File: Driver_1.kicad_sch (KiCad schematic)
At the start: 34 parts

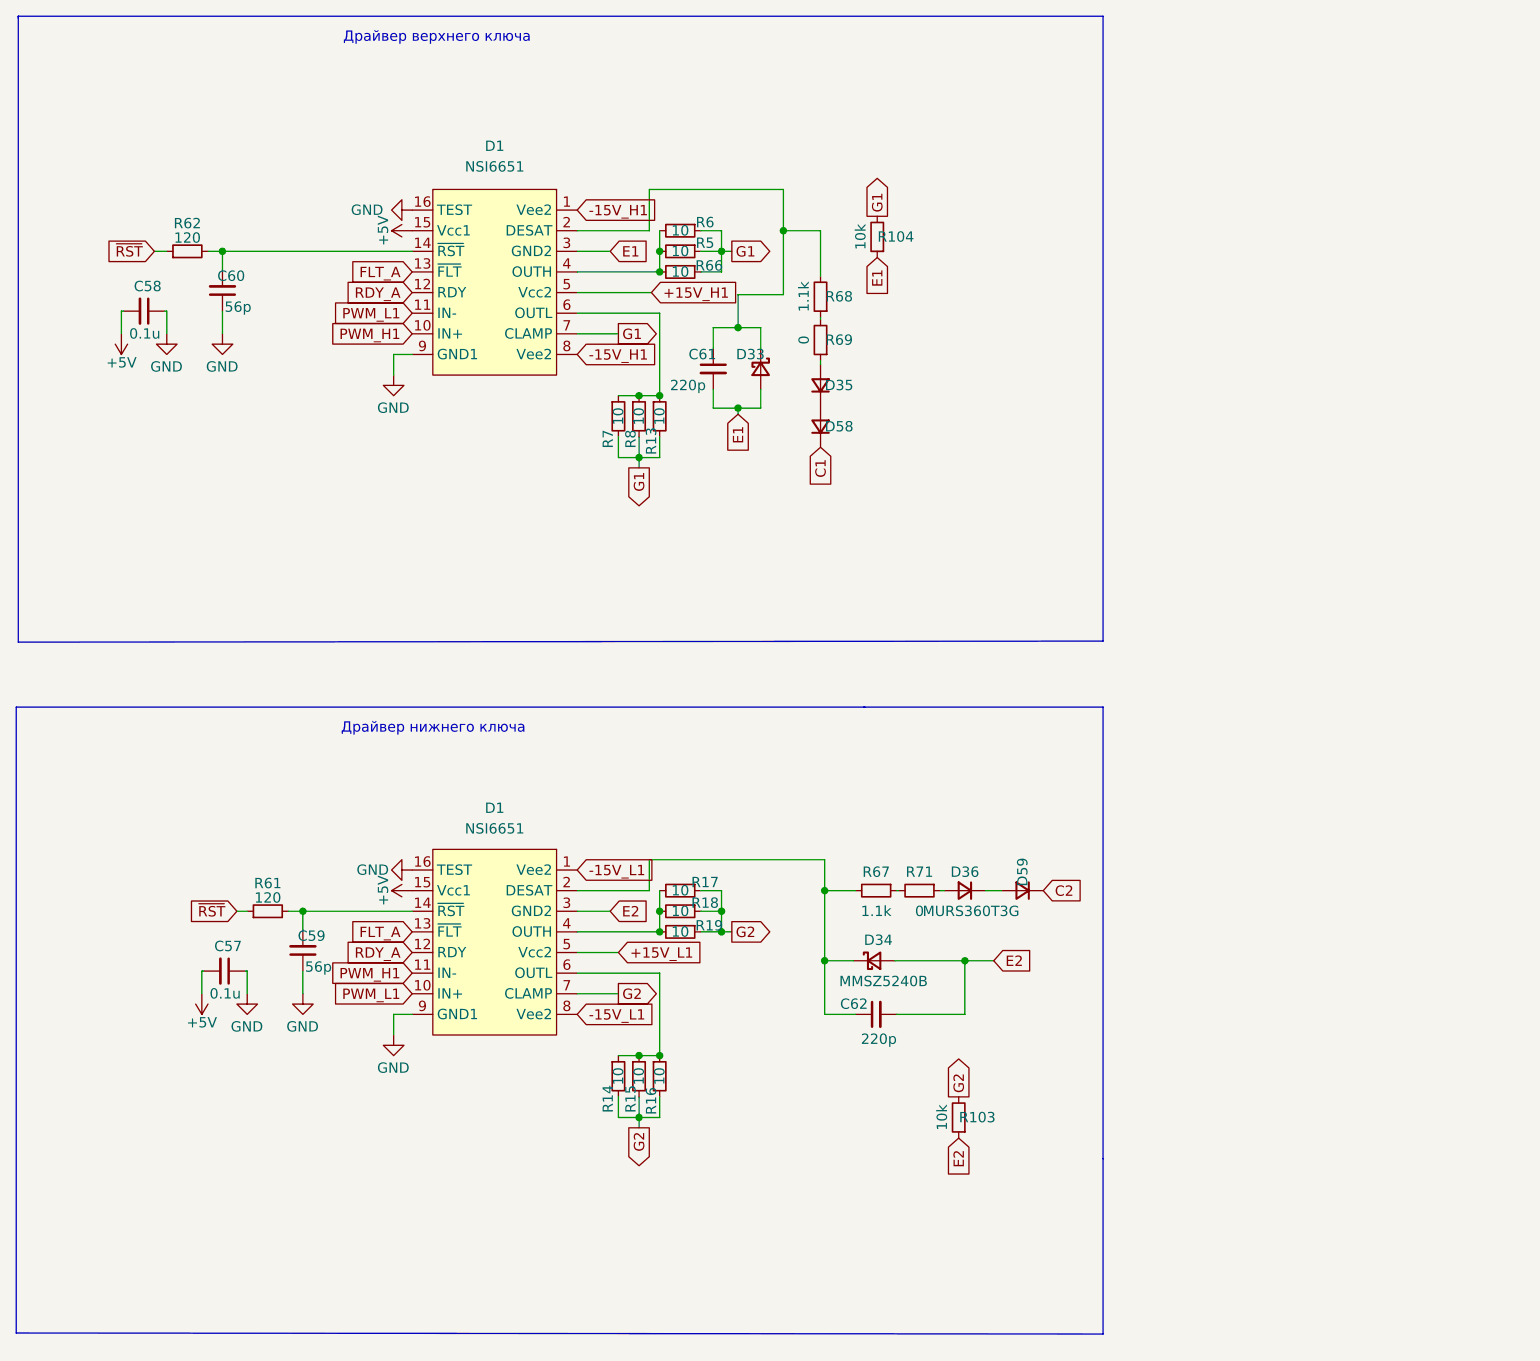
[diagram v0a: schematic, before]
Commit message: Отправил на проверку в резонит: изменил BOM
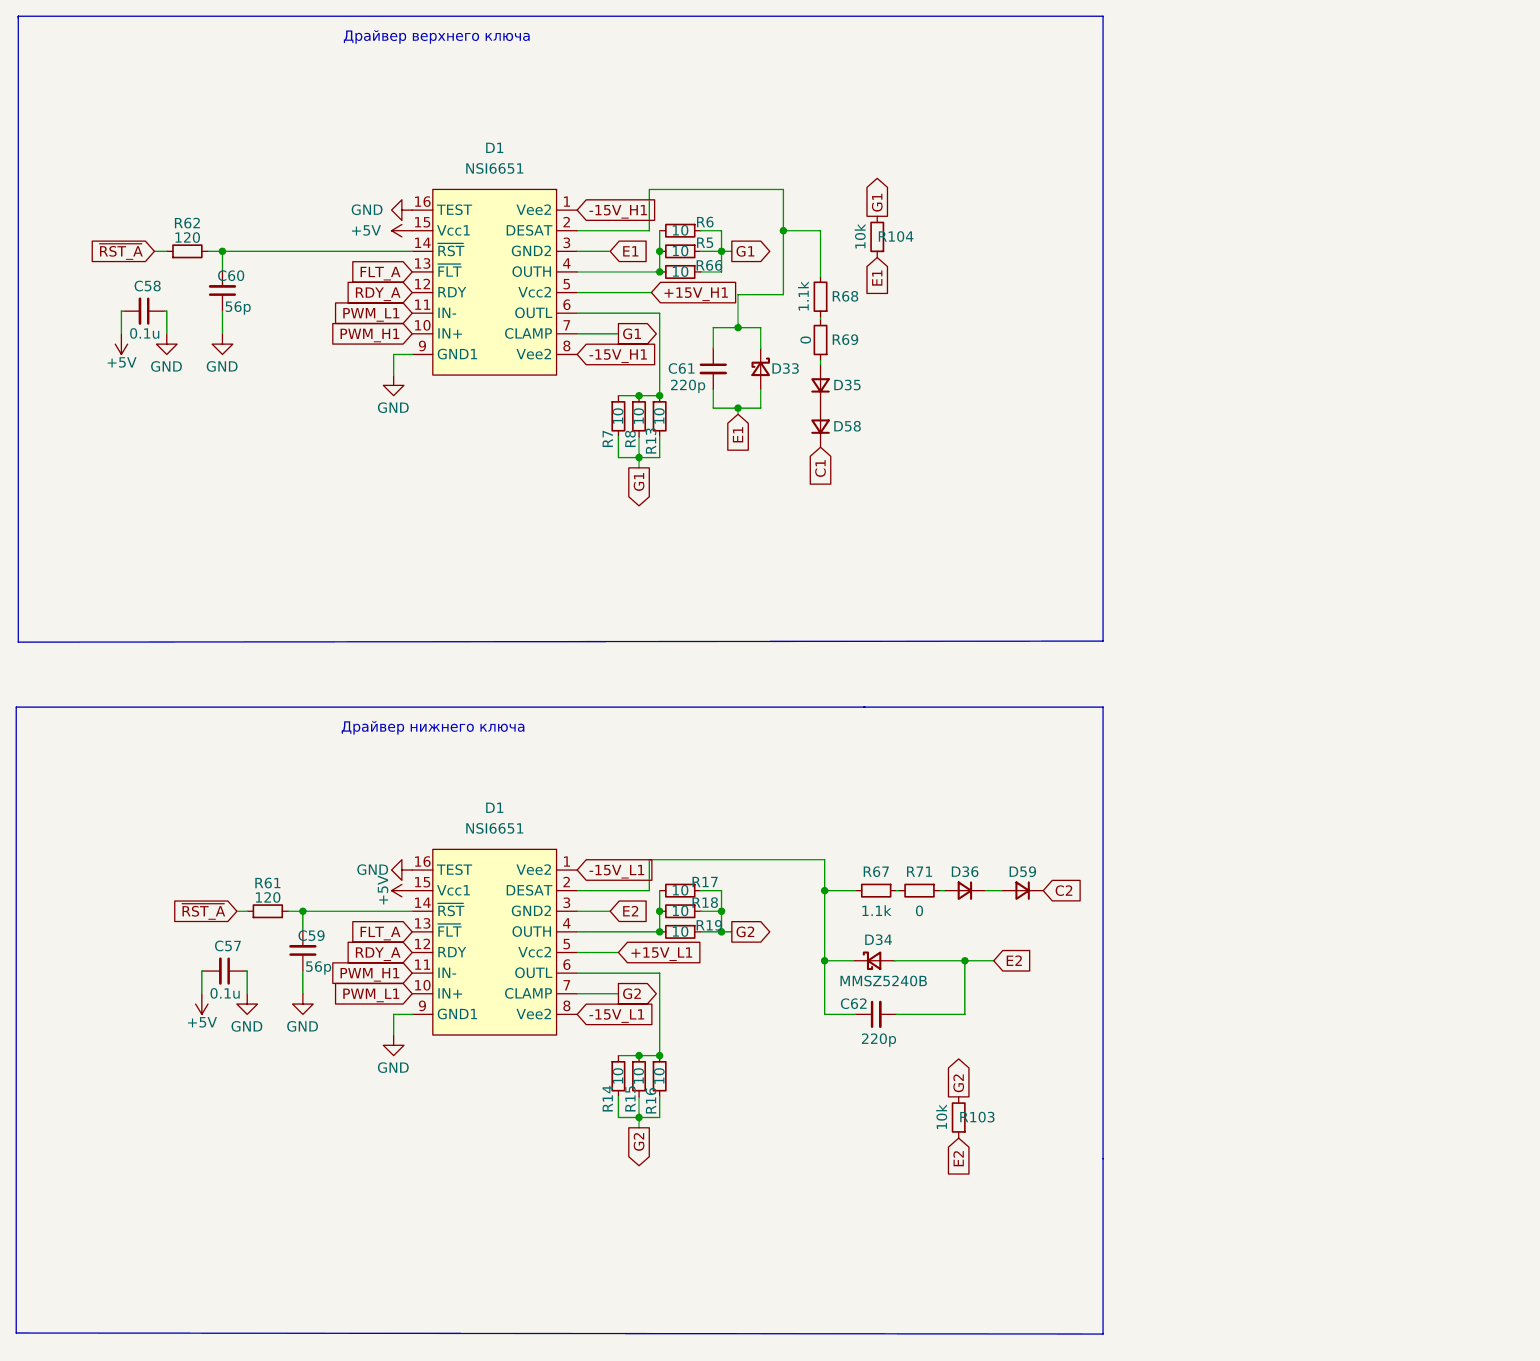
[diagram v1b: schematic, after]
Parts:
- D35, D36, D58, D59: value MURS360T3G -> MURS160
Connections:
- net ~{RST} renamed ~{RST_A}
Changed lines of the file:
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@@
 		)
 	)
-	(global_label "E2"
+	(global_label "~{RST_A}"
 		(shape input)
-		(at 147.32 161.29 270)
+		(at 58.42 133.35 180)
 		(fields_autoplaced yes)
 		(effects
@@
 		)
 		(property "Intersheetrefs" "${INTERSHEET_REFS}"
-			(at 147.2406 166.0617 90)
+			(at 49.9315 133.35 0)
 			(effects
 				(font
@@
 		)
 	)
-	(global_label "E1"
+	(global_label "E2"
 		(shape input)
-		(at 120.142 72.136 270)
+		(at 147.32 161.29 270)
 		(fields_autoplaced yes)
 		(effects
@@
 		)
 		(property "Intersheetrefs" "${INTERSHEET_REFS}"
-			(at 120.0626 76.9077 90)
+			(at 147.2406 166.0617 90)
 			(effects
 				(font
@@
 		)
 	)
-	(global_label "G2"
-		(shape output)
-		(at 147.32 156.21 90)
+	(global_label "E1"
+		(shape input)
+		(at 120.142 72.136 270)
 		(fields_autoplaced yes)
 		(effects
@@
 				(size 1.27 1.27)
 			)
-			(justify left)
+			(justify right)
 		)
 		(property "Intersheetrefs" "${INTERSHEET_REFS}"
-			(at 147.2406 151.3174 90)
+			(at 120.0626 76.9077 90)
 			(effects
 				(font
 					(size 1.27 1.27)
 				)
-				(justify left)
+				(justify right)
 				(hide yes)
 			)
 		)
 	)
-	(global_label "~{RST}"
-		(shape input)
-		(at 48.26 52.07 180)
+	(global_label "G2"
+		(shape output)
+		(at 147.32 156.21 90)
 		(fields_autoplaced yes)
 		(effects
@@
 				(size 1.27 1.27)
 			)
-			(justify right)
+			(justify left)
 		)
 		(property "Intersheetrefs" "${INTERSHEET_REFS}"
-			(at 42.445 52.07 0)
+			(at 147.2406 151.3174 90)
 			(effects
 				(font
 					(size 1.27 1.27)
 				)
-				(justify right)
+				(justify left)
 				(hide yes)
 			)
@@
 		)
 	)
-	(global_label "FLT_A"
+	(global_label "~{RST_A}"
 		(shape input)
-		(at 80.01 54.61 180)
+		(at 48.26 52.07 180)
 		(fields_autoplaced yes)
 		(effects
@@
 		)
 		(property "Intersheetrefs" "${INTERSHEET_REFS}"
-			(at 71.8843 54.61 0)
+			(at 39.7715 52.07 0)
 			(effects
 				(font
@@
 	(global_label "FLT_A"
 		(shape input)
-		(at 80.01 135.89 180)
+		(at 80.01 54.61 180)
 		(fields_autoplaced yes)
 		(effects
@@
 		)
 		(property "Intersheetrefs" "${INTERSHEET_REFS}"
-			(at 71.8843 135.89 0)
+			(at 71.8843 54.61 0)
 			(effects
 				(font
@@
 		)
 	)
-	(global_label "~{RST}"
+	(global_label "FLT_A"
 		(shape input)
-		(at 58.42 133.35 180)
+		(at 80.01 135.89 180)
 		(fields_autoplaced yes)
 		(effects
@@
 		)
 		(property "Intersheetrefs" "${INTERSHEET_REFS}"
-			(at 52.605 133.35 0)
+			(at 71.8843 135.89 0)
 			(effects
 				(font
@@
 		)
 		(property "Value" "+5V"
-			(at 76.454 49.53 0)
+			(at 74.295 49.53 90)
 			(effects
 				(font
@@
 		(fields_autoplaced yes)
 		(property "Reference" "D1"
-			(at 90.17 39.116 0)
+			(at 90.17 39.37 0)
 			(effects
 				(font
@@
 		)
 		(property "Value" "NSI6651"
-			(at 90.17 41.656 0)
+			(at 90.17 41.91 0)
 			(effects
 				(font
@@
 			)
 		)
-		(property "Value" "MURS360T3G"
+		(property "Value" "MURS160"
 			(at 148.844 133.35 0)
 			(effects
@@
 					(size 1.27 1.27)
 				)
+				(hide yes)
 			)
 		)
@@
 		(dnp no)
 		(property "Reference" "D59"
-			(at 155.194 128.524 90)
+			(at 155.194 128.524 0)
 			(effects
 				(font
@@
 			)
 		)
-		(property "Value" "MURS360T3G"
+		(property "Value" "MURS160"
 			(at 155.956 133.35 0)
 			(effects
@@
 		(dnp no)
 		(property "Reference" "D35"
-			(at 132.588 68.58 90)
+			(at 133.604 68.58 90)
 			(effects
 				(font
@@
 			)
 		)
-		(property "Value" "MURS360T3G"
+		(property "Value" "MURS160"
 			(at 127.762 69.342 0)
 			(effects
@@
 		(dnp no)
 		(property "Reference" "R69"
-			(at 132.588 62.992 0)
+			(at 133.35 62.992 0)
 			(effects
 				(font
@@
 		)
 		(property "Value" "0"
-			(at 128.27 62.992 90)
+			(at 128.524 62.992 90)
 			(effects
 				(font
@@
 		(dnp no)
 		(property "Reference" "D58"
-			(at 132.588 73.66 90)
+			(at 133.604 73.66 90)
 			(effects
 				(font
@@
 			)
 		)
-		(property "Value" "MURS360T3G"
+		(property "Value" "MURS160"
 			(at 127.762 74.422 0)
 			(effects
@@
 		(dnp no)
 		(property "Reference" "D33"
-			(at 119.888 64.77 90)
+			(at 124.206 66.548 90)
 			(effects
 				(font
@@
 		(dnp no)
 		(property "Reference" "R68"
-			(at 132.588 57.658 0)
+			(at 133.35 57.658 0)
 			(effects
 				(font
@@
 		(dnp no)
 		(property "Reference" "C61"
-			(at 114.046 64.77 0)
+			(at 111.506 66.548 0)
 			(effects
 				(font

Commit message: Изменения: обновил BOM и названия в схеме
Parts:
- D1: value NSI6651 -> NSI6651ASC-DSWR
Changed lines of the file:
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@@
 			)
 		)
-		(property "Value" "NSI6651"
+		(property "Value" "NSI6651ASC-DSWR"
 			(at 90.17 41.91 0)
 			(effects
@@
 			)
 		)
-		(property "Value" "NSI6651"
+		(property "Value" "NSI6651ASC-DSWR"
 			(at 90.17 123.19 0)
 			(effects

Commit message: Изменения: поменял трассировку полигонов, изменил трассировку цепи DESAT в фазе А
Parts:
- added C90, C91: DNP, Capacitor_SMD:C_0805_2012Metric_Pad1.18x1.45mm_HandSolder, symbol Device:C_Small
- C61, C62: value 220p -> 100p
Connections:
- net E1: now also C90.1
- net E2: now also C91.1
- net G1: now also C90.2
- net G2: now also C91.2
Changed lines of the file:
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@@
 		)
 	)
+	(global_label "G1"
+		(shape output)
+		(at 143.51 47.625 90)
+		(fields_autoplaced yes)
+		(effects
+			(font
+				(size 1.27 1.27)
+			)
+			(justify left)
+		)
+		(property "Intersheetrefs" "${INTERSHEET_REFS}"
+			(at 143.4306 42.7324 90)
+			(effects
+				(font
+					(size 1.27 1.27)
+				)
+				(justify left)
+				(hide yes)
+			)
+		)
+	)
 	(global_label "E1"
 		(shape input)
@@
 	(global_label "E2"
 		(shape input)
+		(at 154.305 161.29 270)
+		(fields_autoplaced yes)
+		(effects
+			(font
+				(size 1.27 1.27)
+			)
+			(justify right)
+		)
+		(property "Intersheetrefs" "${INTERSHEET_REFS}"
+			(at 154.2256 166.0617 90)
+			(effects
+				(font
+					(size 1.27 1.27)
+				)
+				(justify right)
+				(hide yes)
+			)
+		)
+	)
+	(global_label "E2"
+		(shape input)
 		(at 104.394 133.35 0)
 		(fields_autoplaced yes)
@@
 		)
 	)
+	(global_label "G2"
+		(shape output)
+		(at 154.305 156.21 90)
+		(fields_autoplaced yes)
+		(effects
+			(font
+				(size 1.27 1.27)
+			)
+			(justify left)
+		)
+		(property "Intersheetrefs" "${INTERSHEET_REFS}"
+			(at 154.2256 151.3174 90)
+			(effects
+				(font
+					(size 1.27 1.27)
+				)
+				(justify left)
+				(hide yes)
+			)
+		)
+	)
 	(global_label "E1"
 		(shape input)
@@
 		)
 	)
+	(global_label "E1"
+		(shape input)
+		(at 143.51 52.705 270)
+		(fields_autoplaced yes)
+		(effects
+			(font
+				(size 1.27 1.27)
+			)
+			(justify right)
+		)
+		(property "Intersheetrefs" "${INTERSHEET_REFS}"
+			(at 143.5894 57.4767 90)
+			(effects
+				(font
+					(size 1.27 1.27)
+				)
+				(justify right)
+				(hide yes)
+			)
+		)
+	)
 	(global_label "E2"
 		(shape input)
@@
 		(dnp no)
 		(property "Reference" "R103"
-			(at 149.606 158.75 0)
+			(at 149.606 158.75 90)
 			(effects
 				(font
@@
 	)
 	(symbol
+		(lib_id "Device:C_Small")
+		(at 154.305 158.75 180)
+		(unit 1)
+		(exclude_from_sim no)
+		(in_bom yes)
+		(on_board yes)
+		(dnp no)
+		(property "Reference" "C91"
+			(at 159.893 158.75 0)
+			(effects
+				(font
+					(size 1.27 1.27)
+				)
+				(justify left)
+			)
+		)
+		(property "Value" "DNP"
+			(at 159.639 156.718 0)
+			(effects
+				(font
+					(size 1.27 1.27)
+				)
+				(justify left)
+			)
+		)
+		(property "Footprint" "Capacitor_SMD:C_0805_2012Metric_Pad1.18x1.45mm_HandSolder"
+			(at 154.305 158.75 0)
+			(effects
+				(font
+					(size 1.27 1.27)
+				)
+				(hide yes)
+			)
+		)
+		(property "Datasheet" "~"
+			(at 154.305 158.75 0)
+			(effects
+				(font
+					(size 1.27 1.27)
+				)
+				(hide yes)
+			)
+		)
+		(property "Description" "Unpolarized capacitor, small symbol"
+			(at 154.305 158.75 0)
+			(effects
+				(font
+					(size 1.27 1.27)
+				)
+				(hide yes)
+			)
+		)
+		(pin "1"
+		)
+		(pin "2"
+		)
+		(instances
+			(project "Adapter"
+				(path "/e63e39d7-6ac0-4ffd-8aa3-1841a4541b55/24ca47b2-866f-4c90-ba1b-98c358d573e6"
+					(reference "C91")
+					(unit 1)
+				)
+			)
+		)
+	)
+	(symbol
 		(lib_id "Device:D_Schottky_Small")
 		(at 136.906 139.446 0)
@@
 			)
 		)
-		(property "Value" "220p"
+		(property "Value" "100p"
 			(at 139.7 149.098 90)
 			(effects
@@
 	)
 	(symbol
+		(lib_id "Device:C_Small")
+		(at 143.51 50.165 180)
+		(unit 1)
+		(exclude_from_sim no)
+		(in_bom yes)
+		(on_board yes)
+		(dnp no)
+		(property "Reference" "C90"
+			(at 149.098 50.165 0)
+			(effects
+				(font
+					(size 1.27 1.27)
+				)
+				(justify left)
+			)
+		)
+		(property "Value" "DNP"
+			(at 148.844 48.133 0)
+			(effects
+				(font
+					(size 1.27 1.27)
+				)
+				(justify left)
+			)
+		)
+		(property "Footprint" "Capacitor_SMD:C_0805_2012Metric_Pad1.18x1.45mm_HandSolder"
+			(at 143.51 50.165 0)
+			(effects
+				(font
+					(size 1.27 1.27)
+				)
+				(hide yes)
+			)
+		)
+		(property "Datasheet" "~"
+			(at 143.51 50.165 0)
+			(effects
+				(font
+					(size 1.27 1.27)
+				)
+				(hide yes)
+			)
+		)
+		(property "Description" "Unpolarized capacitor, small symbol"
+			(at 143.51 50.165 0)
+			(effects
+				(font
+					(size 1.27 1.27)
+				)
+				(hide yes)
+			)
+		)
+		(pin "1"
+		)
+		(pin "2"
+		)
+		(instances
+			(project "Adapter"
+				(path "/e63e39d7-6ac0-4ffd-8aa3-1841a4541b55/24ca47b2-866f-4c90-ba1b-98c358d573e6"
+					(reference "C90")
+					(unit 1)
+				)
+			)
+		)
+	)
+	(symbol
 		(lib_id "Device:R_Small")
 		(at 52.324 52.07 90)
@@
 			)
 		)
-		(property "Value" "220p"
+		(property "Value" "100p"
 			(at 111.76 68.58 0)
 			(effects

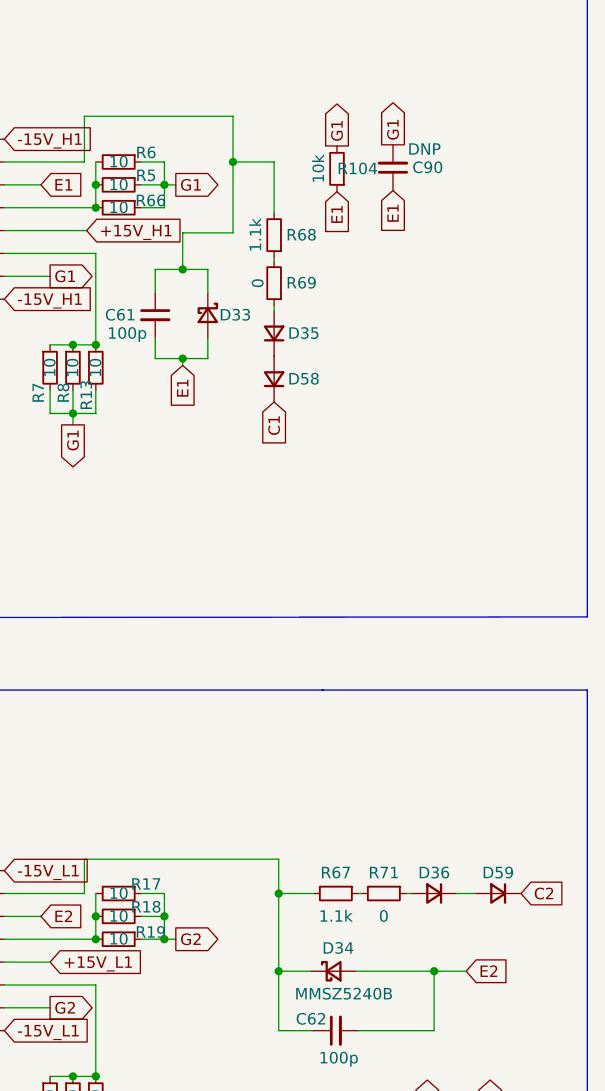
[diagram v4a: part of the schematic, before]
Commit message: VER2.1: переработал цепь DESAT
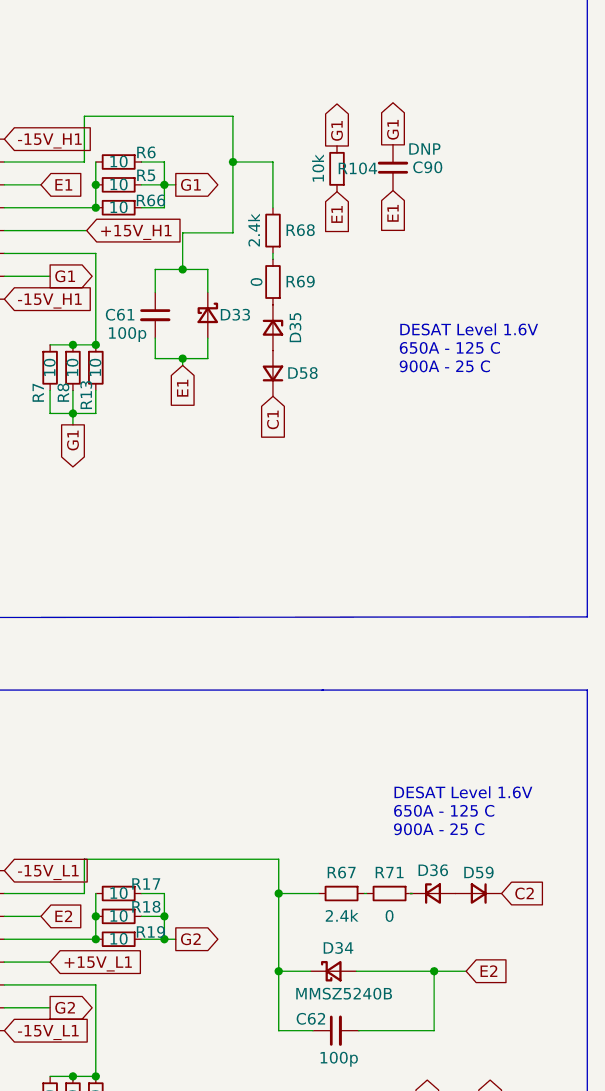
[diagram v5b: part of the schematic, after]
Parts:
- removed D35, D36: MURS160, Diode_SMD:D_SMA_Handsoldering, symbol Device:D_Small
- added D35, D36: MMSZ5232B, Diode_SMD:D_SOD-123, symbol Device:D_Zener_Small
- R67, R68: value 1.1k -> 2.4k
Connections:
- net at R71.1: now also D36.1 (K)
- net at D59.2 (A): now also D36.2 (A)
- net at D58.2 (A): now also D35.2 (A)
- net at R69.1: now also D35.1 (K)
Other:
- note added: "DESAT Level 1.6V 650A - 125 C 900A - 25 C"
- moved on the sheet: D58, D59, R67, R68, R71
